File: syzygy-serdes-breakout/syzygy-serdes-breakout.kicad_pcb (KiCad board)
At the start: 4 copper layers, 50 x 32 mm, 18 parts, among them J1 QTH-020-01-X-D-DP-A, J2 USB3_A, J3 PMOD-2x6-FEMALE, J4 USB3_A_AS_PCIE, SW1 SW_DPDT_x2

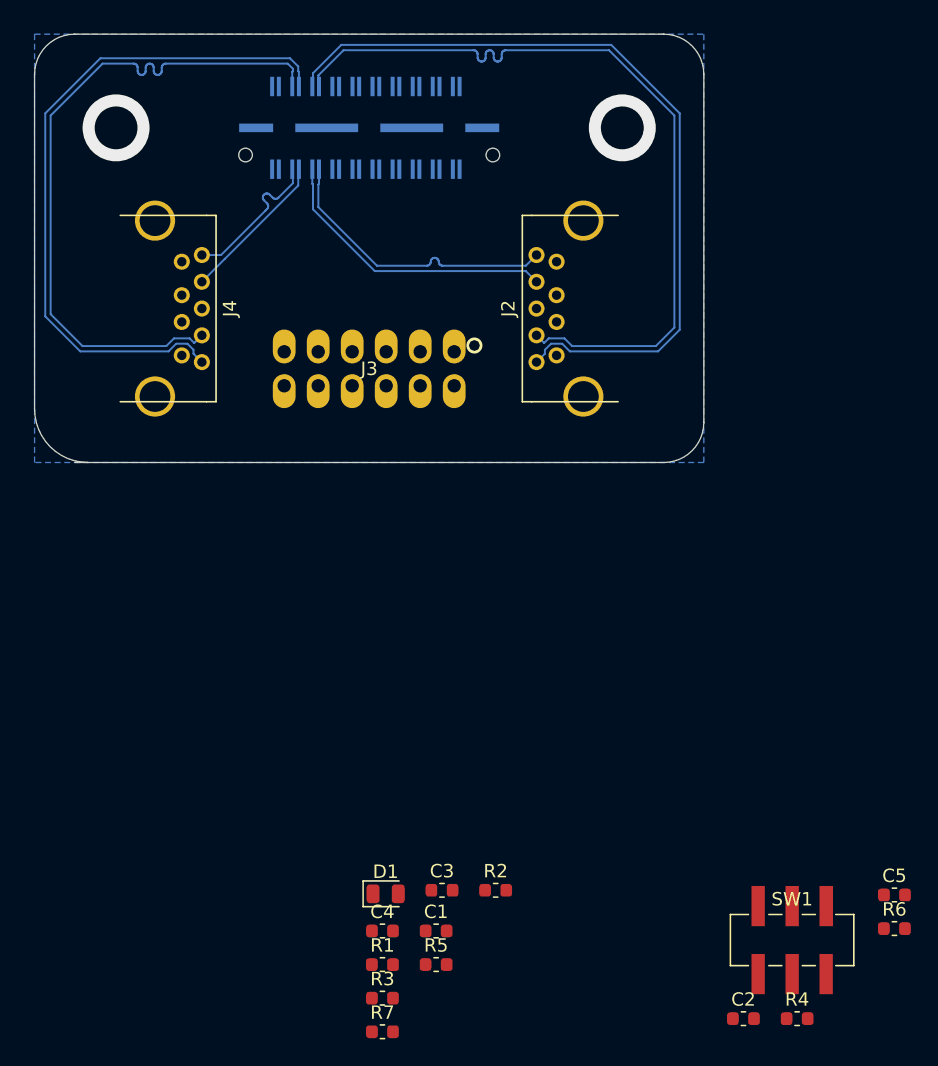
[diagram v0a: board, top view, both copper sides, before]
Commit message: syzygy-serdes-breakout: fix missing ground pour on In1
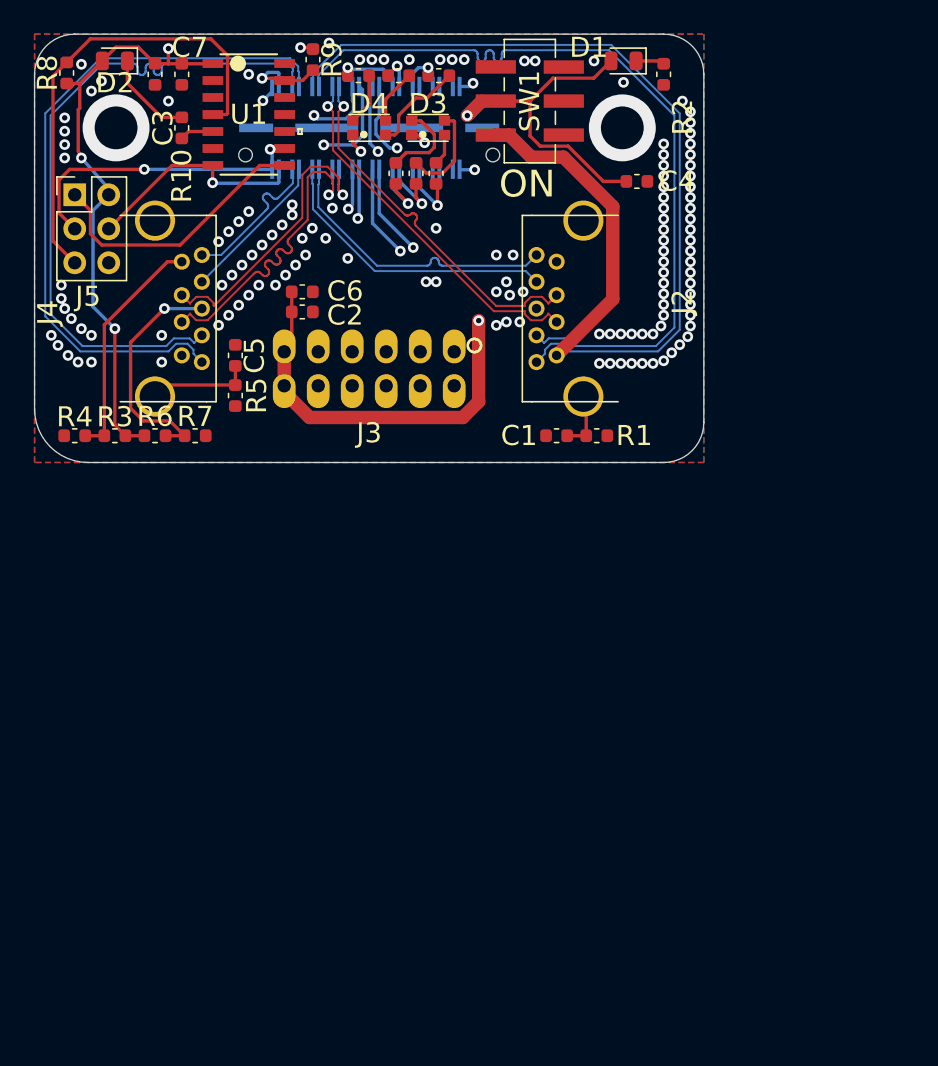
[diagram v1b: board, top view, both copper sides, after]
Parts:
- added C6: 10uF/10V, tom-passives:C_0603_1608Metric, F.Cu at (95.0, 112.2)
- added C7: 0.1uF/10V, tom-passives:C_0603_1608Metric, F.Cu at (86.0, 96.0)
- added D2: LED, tom-opto:LED_0805_2012Metric, F.Cu at (81.0, 95.0)
- added D3: E6C1206RGBC3UDA, tom-opto:E6C1206RGBC3UDA, F.Cu at (104.4, 100.0)
- added D4: E6C1206RGBC3UDA, tom-opto:E6C1206RGBC3UDA, F.Cu at (100.0, 100.0)
- added J5: PMCU_SPI, tom-connectors:PinHeader_2x03_P2.54mm_Vertical, F.Cu at (78.0, 105.0)
- added R10: 1k, tom-passives:R_0603_1608Metric, F.Cu at (86.0, 100.0)
- added R11: 1k2/5%, tom-passives:R_0603_1608Metric, F.Cu at (102.0, 103.4)
- added R12: 300R/5%, tom-passives:R_0603_1608Metric, F.Cu at (103.5, 103.4)
- added R13: 300R/5%, tom-passives:R_0603_1608Metric, F.Cu at (105.0, 103.4)
- added R14: 1k2/5%, tom-passives:R_0603_1608Metric, F.Cu at (99.2, 96.1)
- added R15: 300R/5%, tom-passives:R_0603_1608Metric, F.Cu at (102.2, 96.1)
- added R16: 300R/5%, tom-passives:R_0603_1608Metric, F.Cu at (105.2, 96.1)
- added R8: 10k/1%, tom-passives:C_0603_1608Metric, F.Cu at (77.4, 95.9)
- added R9: 10k/1%, tom-passives:R_0603_1608Metric, F.Cu at (95.8, 94.9)
- added U1: ATTINY44A-SSUR, tom-semiconductors:ATTINY44A-SSUR, F.Cu at (91.0, 99.0)
- R1, R5: value R -> 1M/5%
- moved R4 69.3 mm to (78.0, 123.0), turned to 180 degrees
- moved R6 66.4 mm to (84.0, 123.0)
- moved SW1 65.7 mm to (112.0, 98.0), turned to 90 degrees
- moved D1 64.7 mm to (119.0, 95.0), turned to 180 degrees
- moved C3 64.6 mm to (84.0, 96.0), turned to 270 degrees
- moved C5 63.6 mm to (90.0, 117.0), turned to 270 degrees
- moved C2 62.2 mm to (95.0, 113.8)
- moved R2 62.2 mm to (122.0, 96.0), turned to 270 degrees
- moved C4 59.1 mm to (120.0, 104.0)
- moved R7 46.7 mm to (87.0, 123.0)
- moved R3 46.5 mm to (81.0, 123.0), turned to 180 degrees
- moved R5 45.1 mm to (90.0, 120.0), turned to 90 degrees
- moved R1 42.6 mm to (117.0, 123.0), turned to 180 degrees
- moved C1 38.1 mm to (114.0, 123.0)
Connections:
- net /S0 renamed /S0_N
- net /S1 renamed /S0_P
- C2 pad 1: +3V3 -> VCC
- J1 pad 01: /SCL -> /PMCU_SCK
- J1 pad 03: /SDA -> /PMCU_MOSI
- J1 pad 39: /VIO1 -> VCC
- J3 pad 1: /S3 -> /S9
- J3 pad 10: /S8 -> /S2
- J3 pad 12: +3V3 -> VCC
- J3 pad 2: /S2 -> /S8
- J3 pad 6: +3V3 -> VCC
- J3 pad 9: /S9 -> /S3
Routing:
- net +3V3: track 0.00 -> 70.0 mm, vias 0 -> 5
- net VCC: track 0.00 -> 54.7 mm, vias 0 -> 4
- net +5V: track 0.00 -> 41.3 mm, vias 0 -> 2
- net /PMCU_RESET: track 0.00 -> 34.8 mm
- net /S0_P: track 0.00 -> 27.7 mm, vias 0 -> 1
- net /S0_N: track 0.00 -> 27.7 mm, vias 0 -> 1
- net /S3: track 0.00 -> 27.6 mm, vias 0 -> 1
- net /S7: track 0.00 -> 26.7 mm, vias 0 -> 1
- net /REFCLK_P: track 0.00 -> 25.6 mm, vias 0 -> 1
- net /S5: track 0.00 -> 24.3 mm, vias 0 -> 1
- net Net-(J2-Pad1): track 0.00 -> 23.8 mm
- net /S9: track 0.00 -> 23.1 mm, vias 0 -> 1
- net /PMCU_SCK: track 0.00 -> 23.0 mm, vias 0 -> 2
- net /REFCLK_N: track 0.00 -> 22.6 mm, vias 0 -> 1
- net /SHIELD0: track 0.00 -> 21.7 mm
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- added copper zone on F.Cu, net GND
- added copper zone on In1.Cu, net GND
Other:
- outline, holes or cut-outs redrawn
- board text added: "ON"
- board text added: "dec2020 @TomKeddie"
- board text added: "syzygy serdes breakout"
